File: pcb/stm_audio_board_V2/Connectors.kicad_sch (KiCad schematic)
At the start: 5 parts, among them J3 Audio_sig, J4 Conn_01x10_pots_internal, J6 Conn_01x03_pot_ext, J8 GuitarOUT_R, J9 GuitarOUT_L

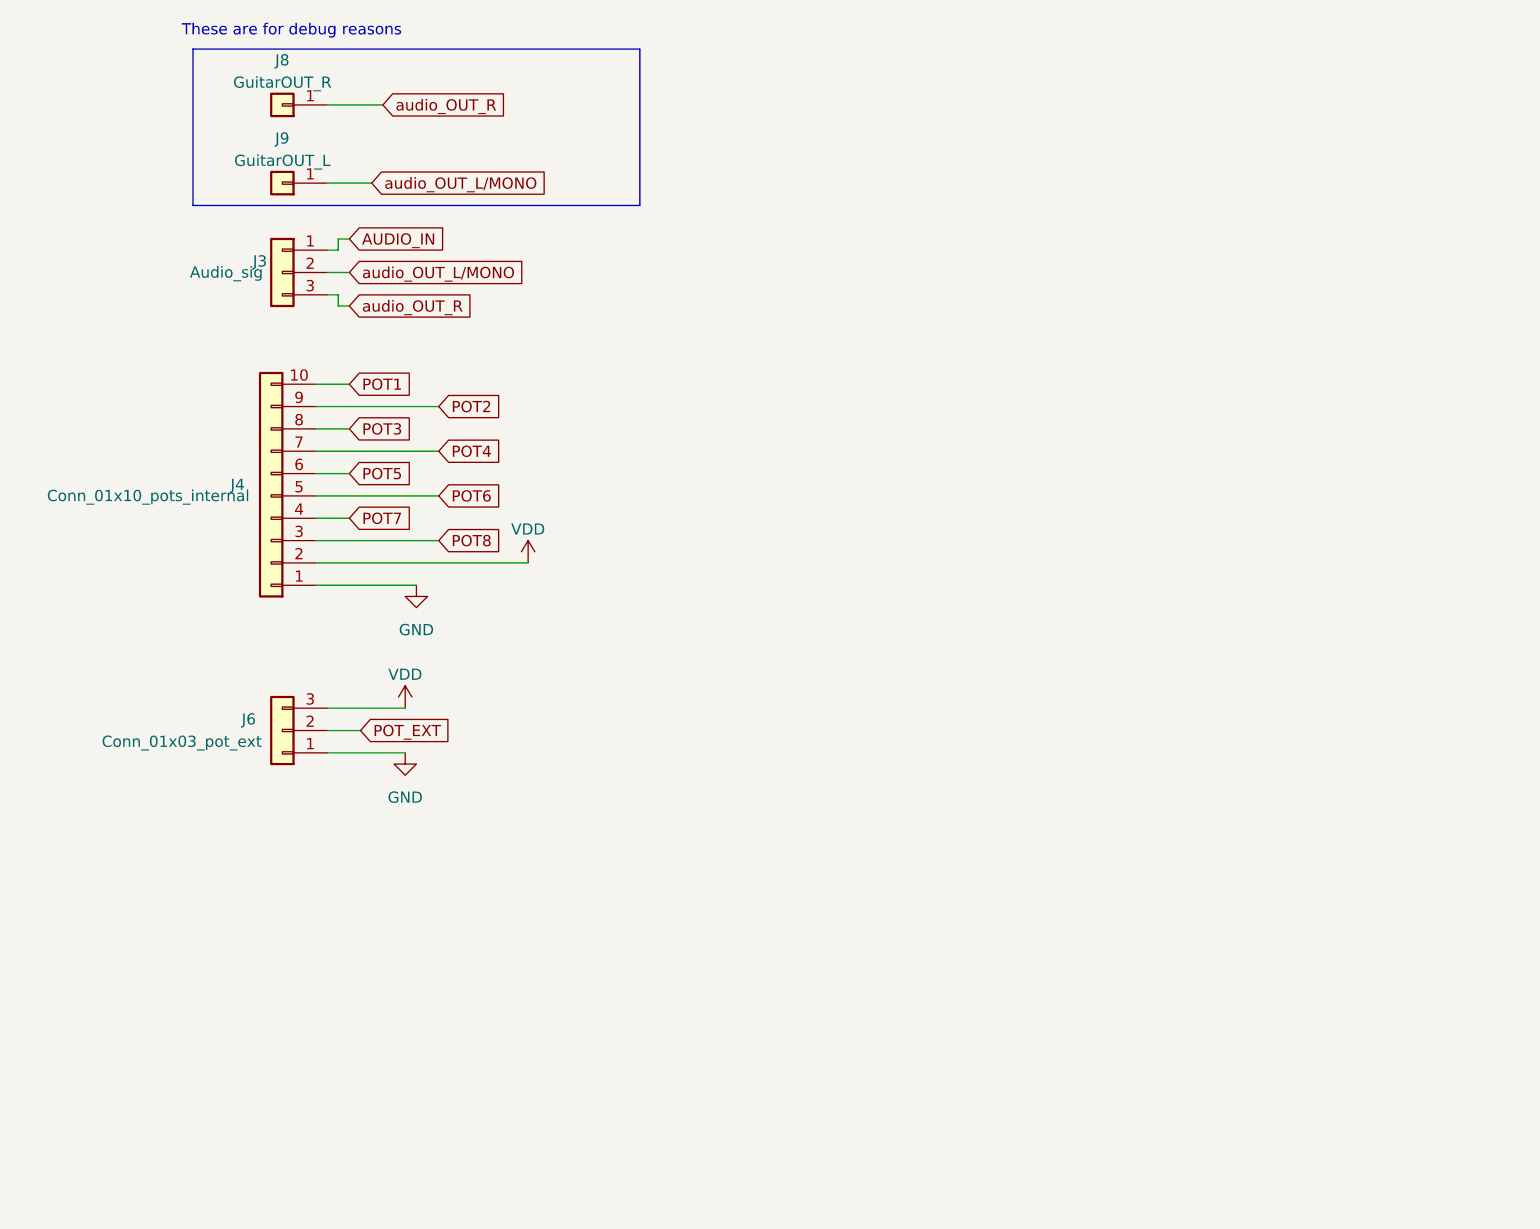
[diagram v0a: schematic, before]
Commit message: added choke to analog pwr, created 5 V rail, decided to pivot and use codec instead dedicated hardware
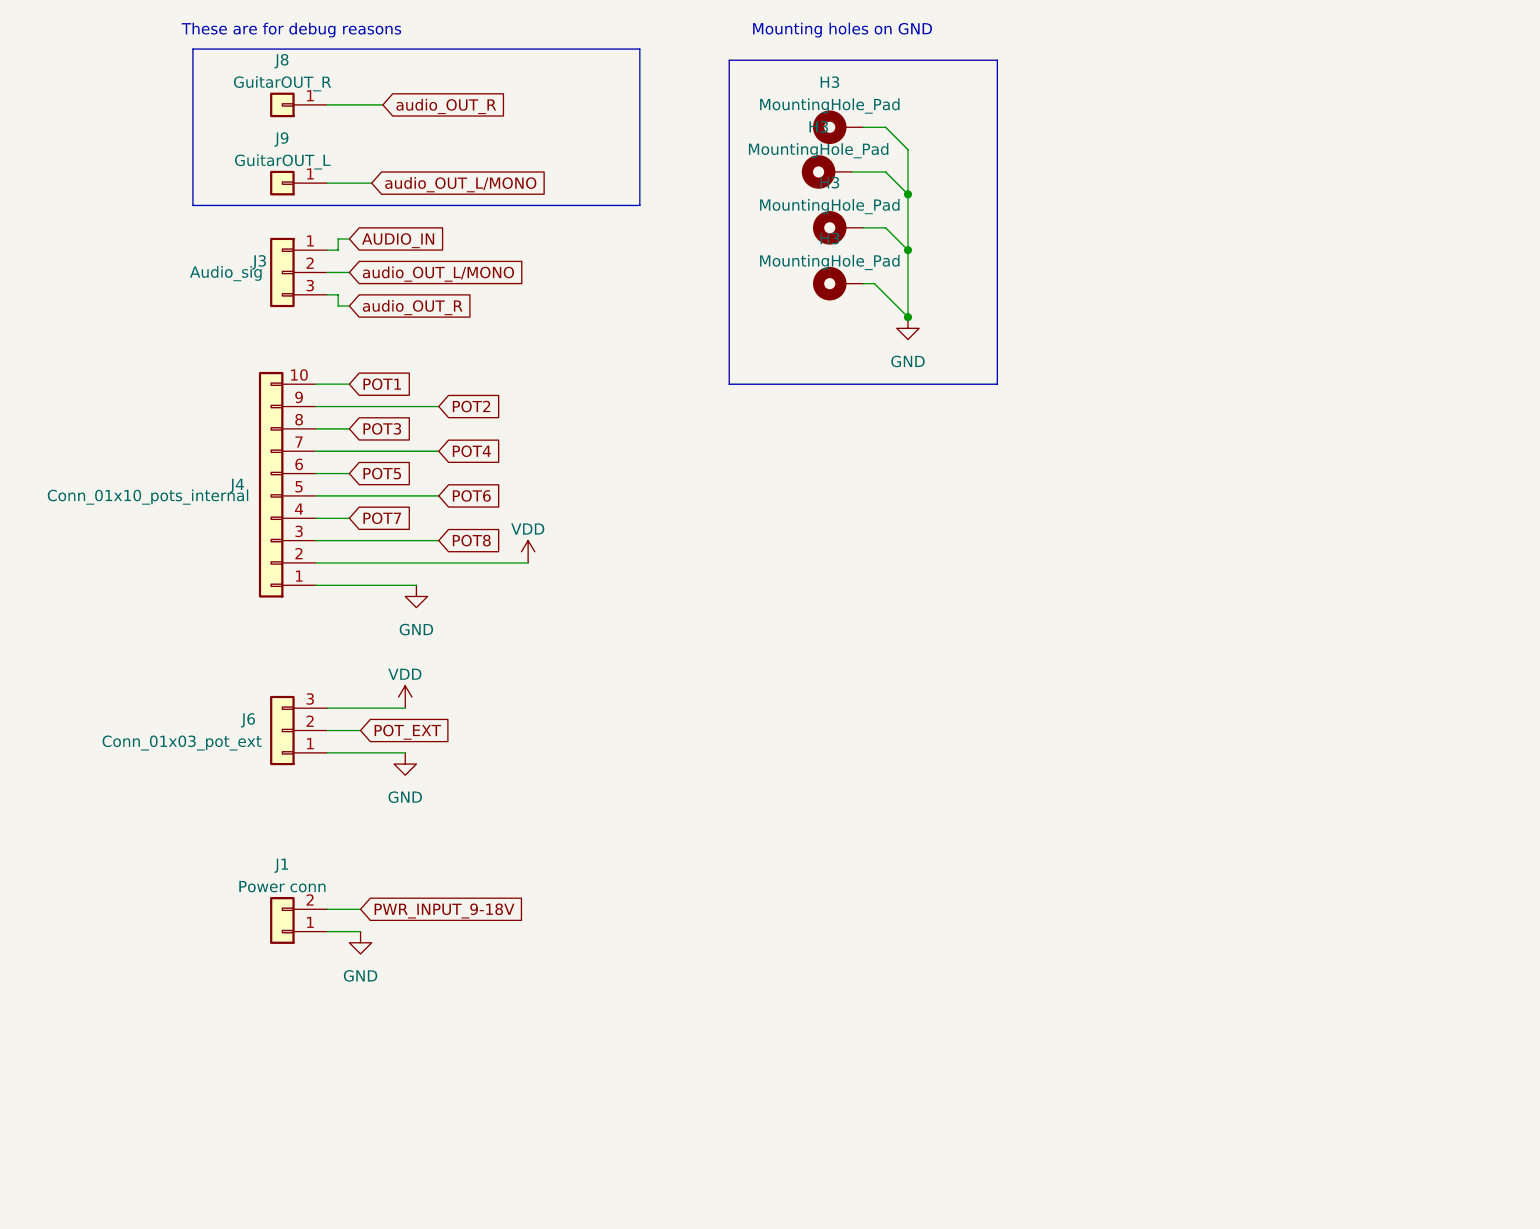
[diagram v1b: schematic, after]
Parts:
- added H3 (x4): MountingHole_Pad, MountingHole:MountingHole_3.2mm_M3_DIN965_Pad, symbol Mechanical:MountingHole_Pad
- added J1: Power conn, Connector_PinHeader_2.54mm:PinHeader_1x02_P2.54mm_Vertical, symbol Connector_Generic:Conn_01x02
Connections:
- net GND: now also H3.1, H3.1, H3.1, H3.1, J1.1 (Pin_1)
- new net PWR_INPUT_9-18V: J1.2 (Pin_2)
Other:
- note added: "Mounting holes on GND"

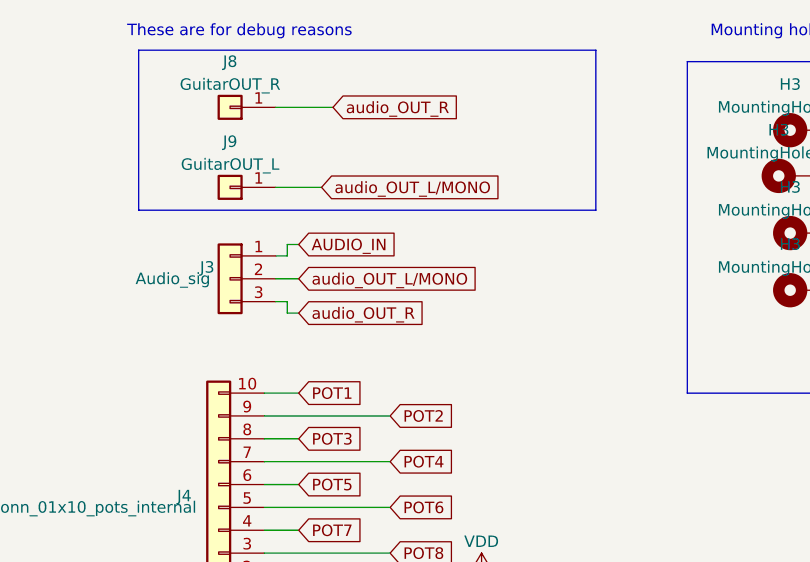
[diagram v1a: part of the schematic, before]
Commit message: testing offset sim, and changing layout
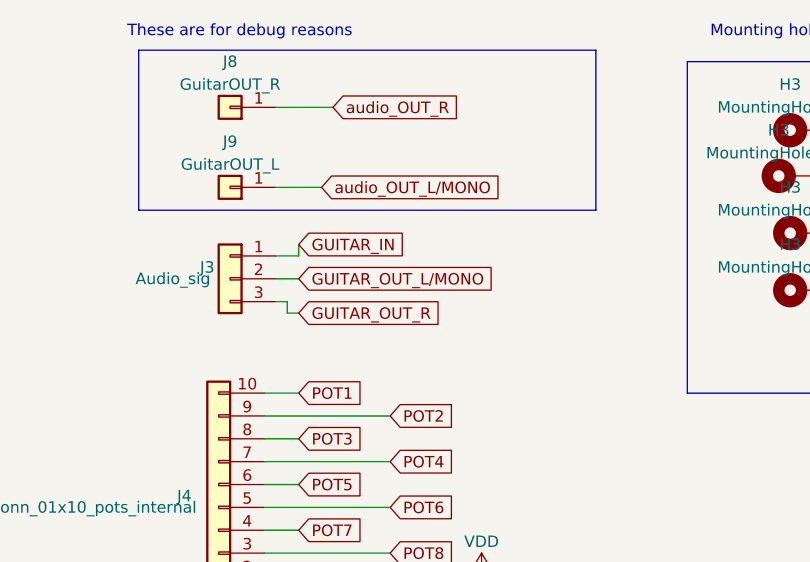
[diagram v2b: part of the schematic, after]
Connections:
- net audio_OUT_L/MONO: no longer J3.2 (Pin_2)
- net audio_OUT_R: no longer J3.3 (Pin_3)
- net AUDIO_IN renamed GUITAR_IN
- new net GUITAR_OUT_L/MONO: J3.2 (Pin_2)
- new net GUITAR_OUT_R: J3.3 (Pin_3)
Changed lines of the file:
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@@
     (stroke (width 0) (type default))
   )
-  (wire (pts (xy 48.26 46.99) (xy 46.99 46.99))
+  (wire (pts (xy 49.53 46.99) (xy 46.99 46.99))
     (stroke (width 0) (type default))
   )
@@
     (stroke (width 0) (type default))
   )
-  (wire (pts (xy 48.26 45.72) (xy 48.26 46.99))
+  (wire (pts (xy 49.53 45.72) (xy 49.53 46.99))
     (stroke (width 0) (type default))
   )
@@
   )
   (wire (pts (xy 110.49 33.02) (xy 113.03 35.56))
-    (stroke (width 0) (type default))
-  )
-  (wire (pts (xy 48.26 45.72) (xy 49.53 45.72))
     (stroke (width 0) (type default))
   )
@@
     )
   )
-  (global_label "AUDIO_IN" (shape input) (at 49.53 45.72 0) (fields_autoplaced)
+  (global_label "GUITAR_OUT_L{slash}MONO" (shape input) (at 49.53 49.53 0) (fields_autoplaced)
     (effects (font (size 1.27 1.27)) (justify left))
-    (property "Intersheetrefs" "${INTERSHEET_REFS}" (at 60.9631 45.72 0)
-      (effects (font (size 1.27 1.27)) (justify left) hide)
-    )
-  )
-  (global_label "audio_OUT_L{slash}MONO" (shape input) (at 49.53 49.53 0) (fields_autoplaced)
-    (effects (font (size 1.27 1.27)) (justify left))
-    (property "Intersheetrefs" "${INTERSHEET_REFS}" (at 71.0019 49.53 0)
+    (property "Intersheetrefs" "${INTERSHEET_REFS}" (at 72.3326 49.53 0)
       (effects (font (size 1.27 1.27)) (justify left) hide)
     )
@@
     )
   )
-  (global_label "audio_OUT_R" (shape input) (at 49.53 53.34 0) (fields_autoplaced)
+  (global_label "GUITAR_OUT_R" (shape input) (at 49.53 53.34 0) (fields_autoplaced)
     (effects (font (size 1.27 1.27)) (justify left))
-    (property "Intersheetrefs" "${INTERSHEET_REFS}" (at 64.4704 53.34 0)
+    (property "Intersheetrefs" "${INTERSHEET_REFS}" (at 65.8011 53.34 0)
       (effects (font (size 1.27 1.27)) (justify left) hide)
     )
@@
       (effects (font (size 1.27 1.27)) (justify left) hide)
     )
+  )
+  (global_label "GUITAR_IN" (shape input) (at 49.53 45.72 0) (fields_autoplaced)
+    (effects (font (size 1.27 1.27)) (justify left))
+    (property "Intersheetrefs" "${INTERSHEET_REFS}" (at 61.8702 45.72 0)
+      (effects (font (size 1.27 1.27)) (justify left) hide)
+    )

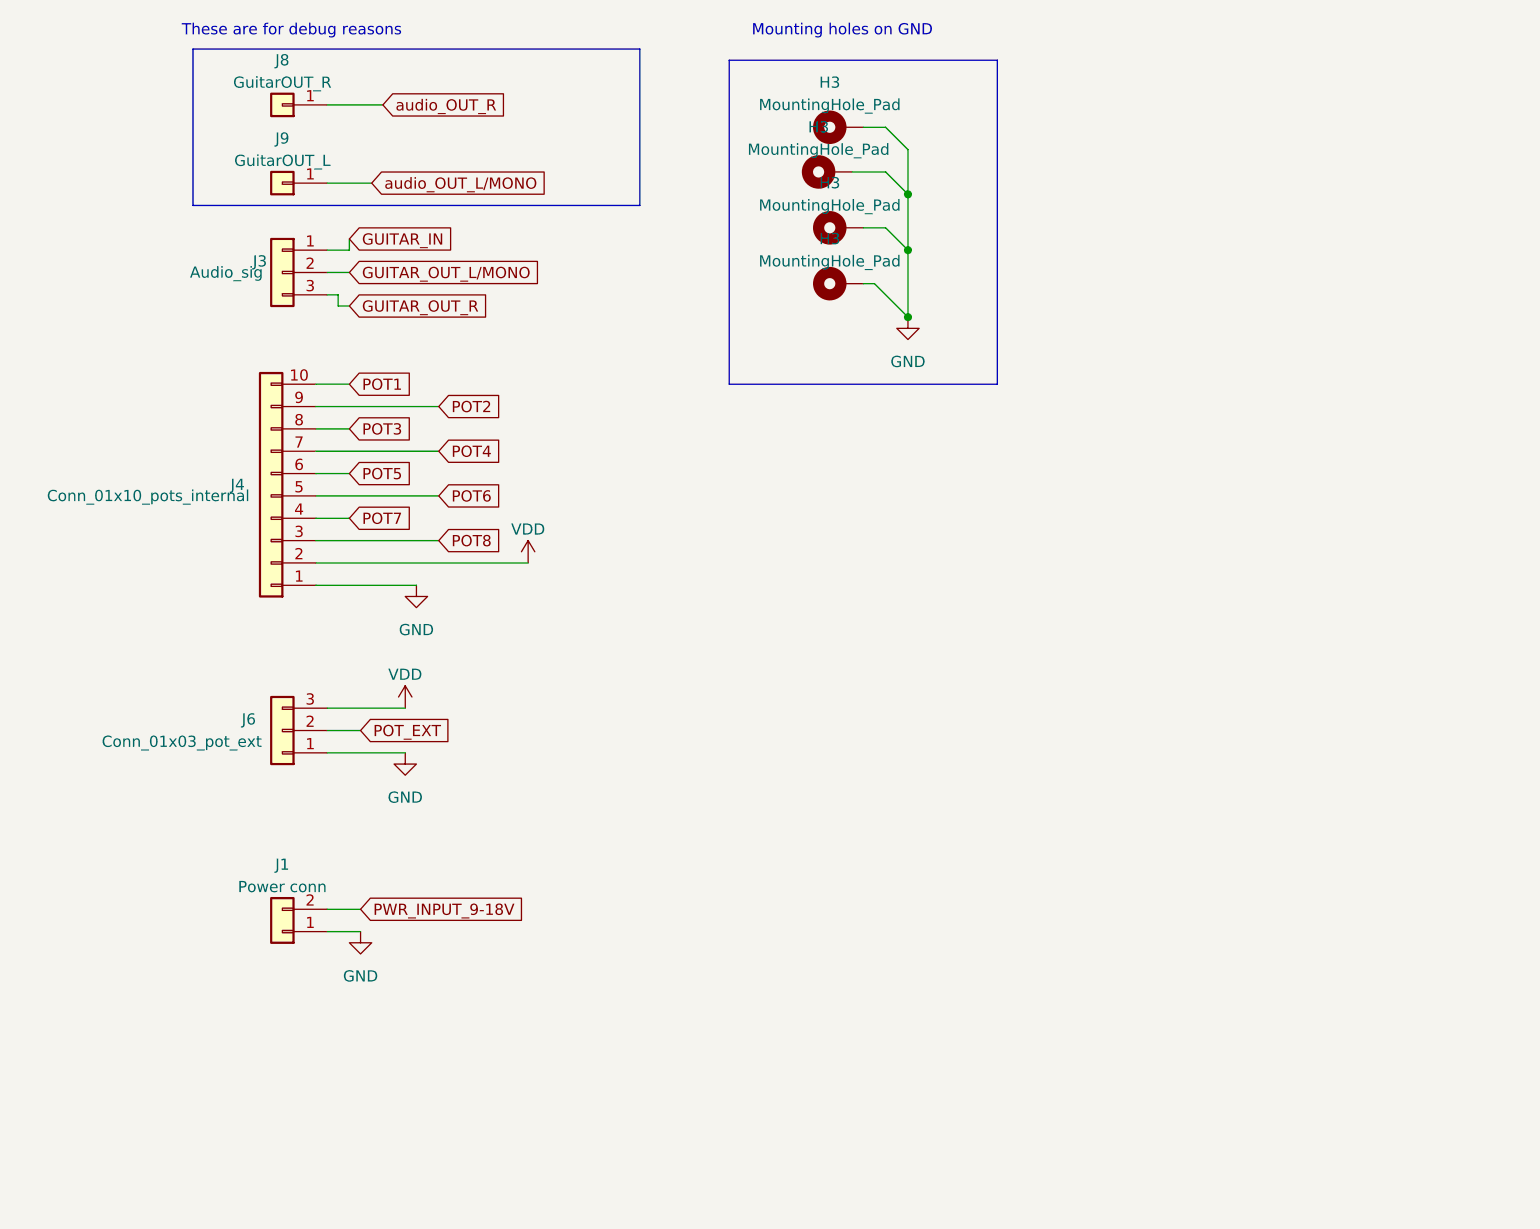
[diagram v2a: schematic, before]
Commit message: input and output stage reworked in sim and in schematic, power filtering is changed, further calculations needed
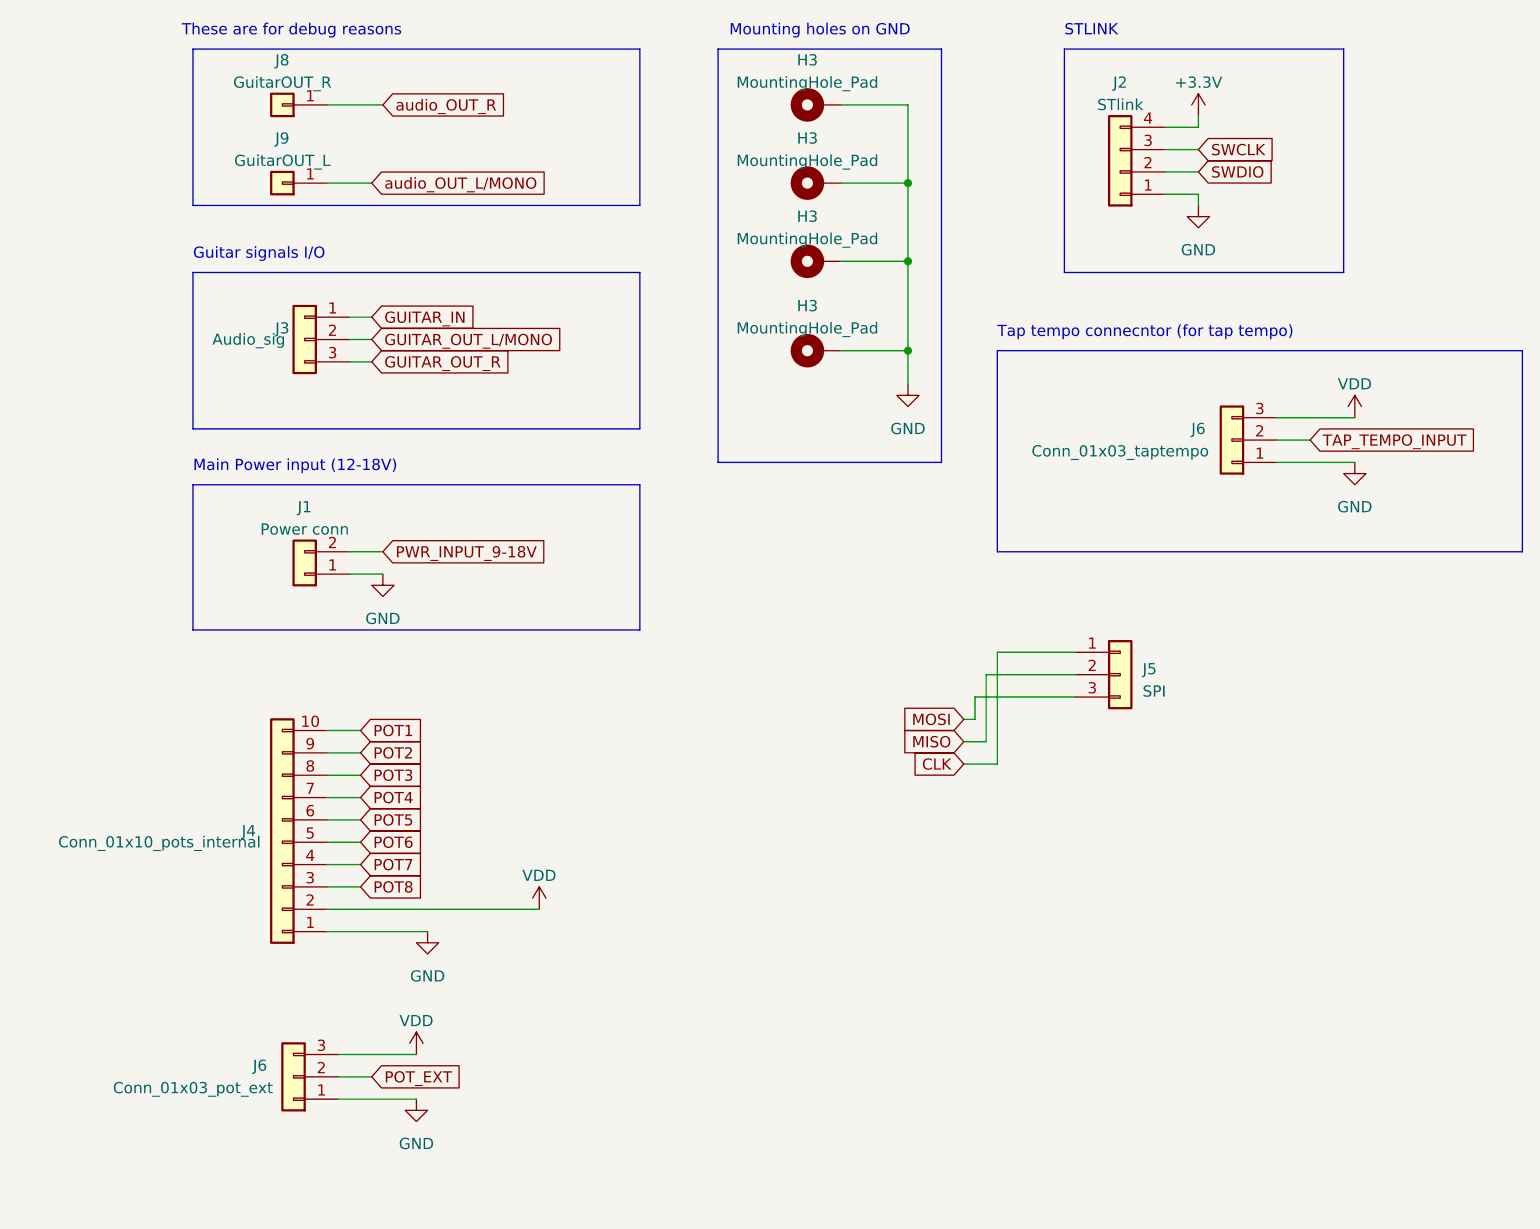
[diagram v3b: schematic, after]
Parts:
- added J2: STlink, Connector_PinHeader_2.54mm:PinHeader_1x04_P2.54mm_Vertical, symbol Connector_Generic:Conn_01x04
- added J5: SPI, Connector_PinHeader_2.54mm:PinHeader_1x03_P2.54mm_Vertical, symbol Connector_Generic:Conn_01x03
- added J6: Conn_01x03_taptempo, Connector_PinHeader_2.54mm:PinHeader_1x03_P2.54mm_Vertical, symbol Connector_Generic:Conn_01x03
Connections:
- net GND: now also J2.1 (Pin_1), J6.1 (Pin_1)
- net VDD: now also J6.3 (Pin_3)
- new net +3.3V: J2.4 (Pin_4)
- new net CLK: J5.1 (Pin_1)
- new net MISO: J5.2 (Pin_2)
- new net MOSI: J5.3 (Pin_3)
- new net SWCLK: J2.3 (Pin_3)
- new net SWDIO: J2.2 (Pin_2)
- new net TAP_TEMPO_INPUT: J6.2 (Pin_2)
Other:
- note added: "Guitar signals I/O"
- note added: "Main Power input (12-18V)"
- note added: "STLINK"
- note added: "Tap tempo connecntor (for tap tempo)"
- moved on the sheet: H3, J1, J3, J4, J6
